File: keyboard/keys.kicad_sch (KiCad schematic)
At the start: 112 parts, among them SW1 SW_Push, SW10 SW_Push, SW11 SW_Push, SW12 SW_Push, SW13 SW_Push, SW14 SW_Push, SW15 SW_Push, SW16 SW_Push, SW17 SW_Push, SW18 SW_Push, SW19 SW_Push, SW2 SW_Push, SW20 SW_Push, SW21 SW_Push, SW22 SW_Push, SW23 SW_Push, SW24 SW_Push, SW25 SW_Push, SW26 SW_Push, SW27 SW_Push, SW28 SW_Push, SW29 SW_Push, SW3 SW_Push, SW30 SW_Push, SW31 SW_Push, SW32 SW_Push, SW33 SW_Push, SW34 SW_Push, SW35 SW_Push, SW36 SW_Push, SW37 SW_Push, SW38 SW_Push, SW39 SW_Push, SW4 SW_Push, SW40 SW_Push, SW41 SW_Push, SW42 SW_Push, SW43 SW_Push, SW44 SW_Push, SW45 SW_Push, SW46 SW_Push, SW47 SW_Push, SW48 SW_Push, SW49 SW_Push, SW5 SW_Push, SW50 SW_Push, SW51 SW_Push, SW52 SW_Push, SW53 SW_Push, SW54 SW_Push, SW55 SW_Push, SW56 SW_Push, SW6 SW_Push, SW7 SW_Push, SW8 SW_Push, SW9 SW_Push

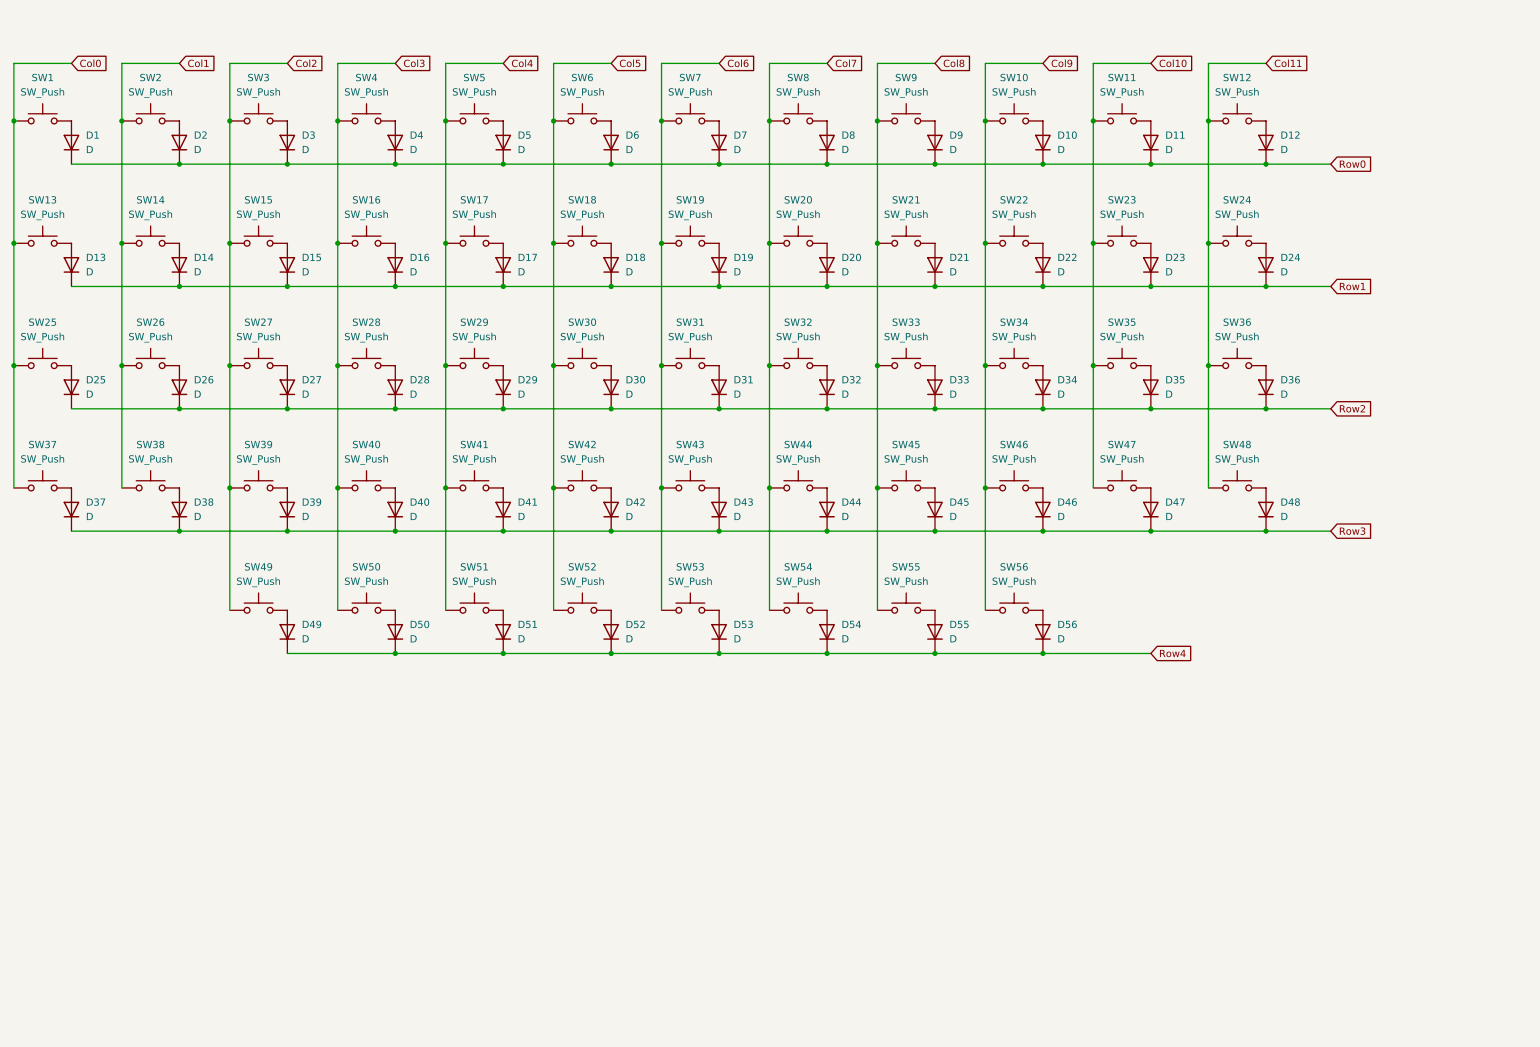
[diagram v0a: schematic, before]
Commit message: Add 3dshapes, footprint library, symbol library, and display mixer board.
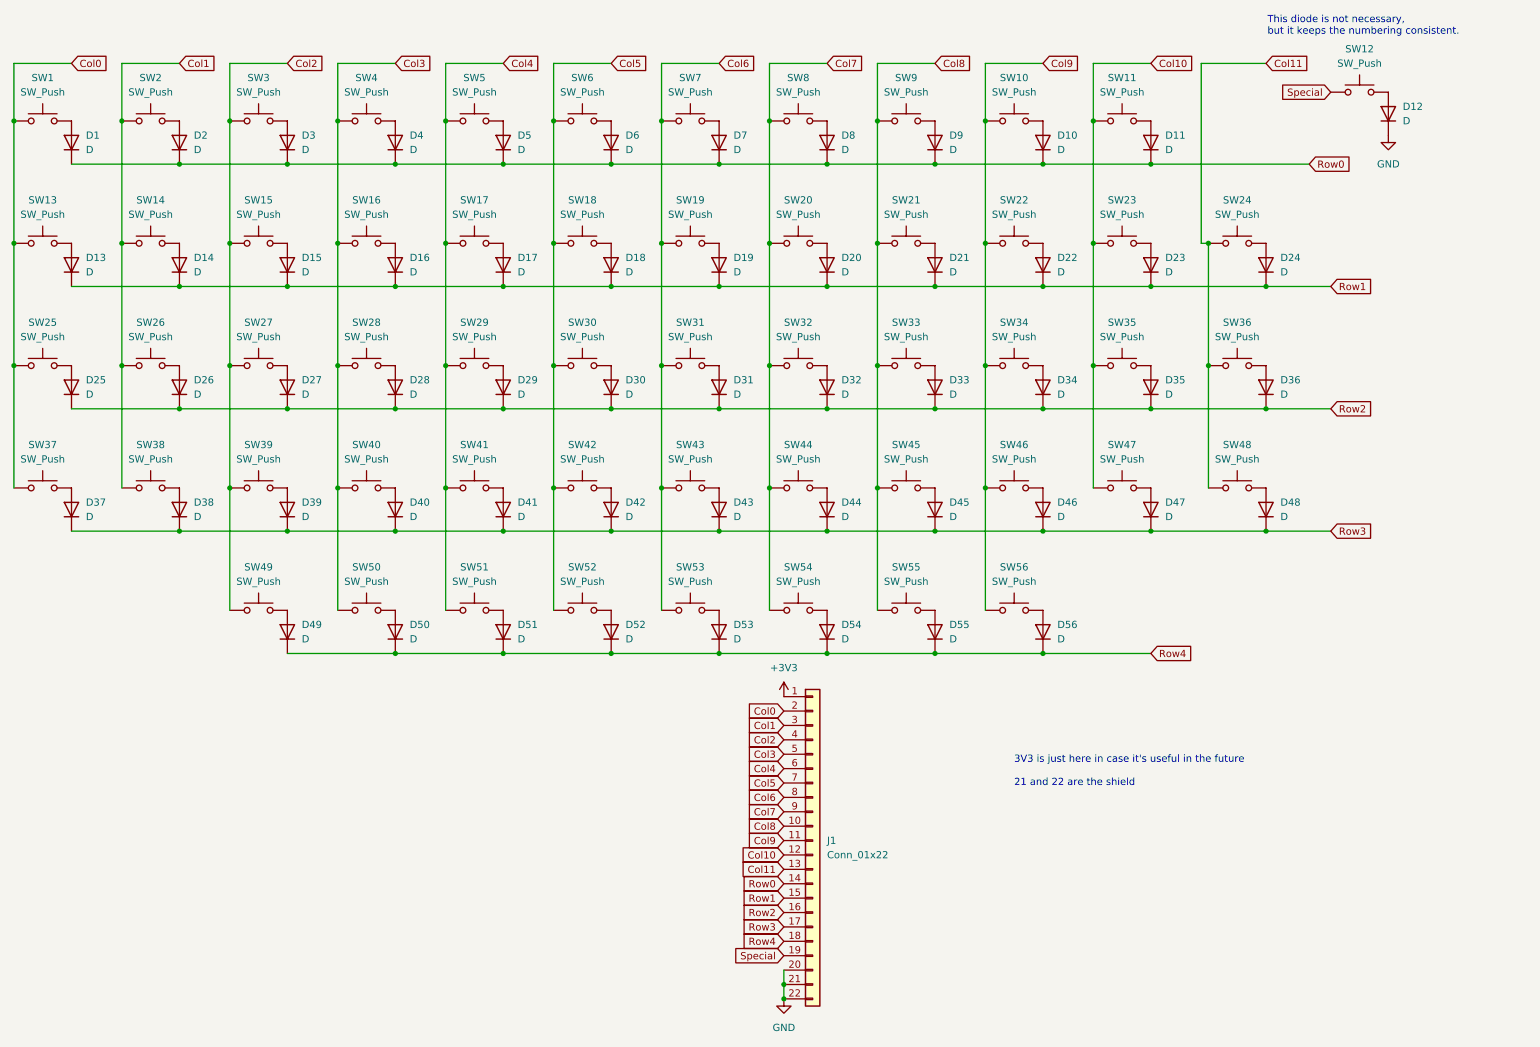
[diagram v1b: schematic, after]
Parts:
- added J1: Conn_01x22, kirdos:JUSHOU_AFC07-S20FCC-00-FPC-SMD_0.5P, symbol Connector_Generic:Conn_01x22
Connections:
- net Col0: now also J1.2 (Pin_2)
- net Col1: now also J1.3 (Pin_3)
- net Col10: now also J1.12 (Pin_12)
- net Col11: now also J1.13 (Pin_13); no longer SW12.1
- net Col2: now also J1.4 (Pin_4)
- net Col3: now also J1.5 (Pin_5)
- net Col4: now also J1.6 (Pin_6)
- net Col5: now also J1.7 (Pin_7)
- net Col6: now also J1.8 (Pin_8)
- net Col7: now also J1.9 (Pin_9)
- net Col8: now also J1.10 (Pin_10)
- net Col9: now also J1.11 (Pin_11)
- net Row0: now also J1.14 (Pin_14); no longer D12.1 (K)
- net Row1: now also J1.15 (Pin_15)
- net Row2: now also J1.16 (Pin_16)
- net Row3: now also J1.17 (Pin_17)
- net Row4: now also J1.18 (Pin_18)
- new net +3V3: J1.1 (Pin_1)
- new net GND: D12.1 (K), J1.20 (Pin_20), J1.21 (Pin_21), J1.22 (Pin_22)
- new net Special: J1.19 (Pin_19), SW12.1
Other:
- note added: "3V3 is just here in case it's useful in the future 21 and 22 are the shield"
- note added: "This diode is not necessary, but it keeps the numbering consistent."
- moved on the sheet: SW12
